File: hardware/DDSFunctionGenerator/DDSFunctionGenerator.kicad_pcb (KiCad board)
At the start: 2 copper layers, 100 x 100 mm, 83 parts, among them J1 Conn_Coaxial, Q1 Q_NPN_BEC, Q2 Q_NPN_BEC, Q3 Q_NPN_BEC, U1 TC1107-3.3VOA, U2 L7805, U3 L7805, U4 AD9832, U5 STM32F030K6Tx, Y1 Crystal

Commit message: draft of an amplifier
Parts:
- added C26: 100n, Capacitor_SMD:C_0805_2012Metric_Pad1.15x1.40mm_HandSolder, F.Cu at (95.0, 145.0)
- added C27: 100n, Capacitor_SMD:C_0805_2012Metric_Pad1.15x1.40mm_HandSolder, F.Cu at (97.6, 98.0)
- added C28: 100n, Capacitor_SMD:C_0805_2012Metric_Pad1.15x1.40mm_HandSolder, F.Cu at (92.9, 98.0)
- added C29: 100n, Capacitor_SMD:C_0805_2012Metric_Pad1.15x1.40mm_HandSolder, F.Cu at (92.9, 100.9)
- added C30: 100n, Capacitor_SMD:C_0805_2012Metric_Pad1.15x1.40mm_HandSolder, F.Cu at (92.9, 103.9)
- added C31: 100n, Capacitor_SMD:C_0805_2012Metric_Pad1.15x1.40mm_HandSolder, F.Cu at (102.4, 98.0)
- added C32: 100n, Capacitor_SMD:C_0805_2012Metric_Pad1.15x1.40mm_HandSolder, F.Cu at (100.0, 108.0)
- added C33: 100n, Capacitor_SMD:C_0805_2012Metric_Pad1.15x1.40mm_HandSolder, F.Cu at (107.3, 103.0)
- added C34: 100n, Capacitor_SMD:C_0805_2012Metric_Pad1.15x1.40mm_HandSolder, F.Cu at (104.8, 108.0)
- added C35: 100n, Capacitor_SMD:C_0805_2012Metric_Pad1.15x1.40mm_HandSolder, F.Cu at (109.5, 106.0)
- added C36: 100n, Capacitor_SMD:C_0805_2012Metric_Pad1.15x1.40mm_HandSolder, F.Cu at (109.5, 109.0)
- added D4: LED, LED_SMD:LED_0805_2012Metric, F.Cu at (99.6, 145.0)
- added J2: USB_B_Micro, Connector_USB:USB_Micro-B_Molex_47346-0001, F.Cu at (97.8, 139.1)
- added L9: 4u7, Inductor_SMD:L_1812_4532Metric_Pad1.30x3.40mm_HandSolder, F.Cu at (101.3, 104.0)
- added R31: 510R, Resistor_SMD:R_0805_2012Metric_Pad1.15x1.40mm_HandSolder, F.Cu at (105.2, 142.1)
- added SW1: Rotary_Encoder_Switch, Rotary_Encoder:RotaryEncoder_Alps_EC12E-Switch_Vertical_H20mm, F.Cu at (94.7, 121.2)
- added U6: FT200XD, Package_DFN_QFN:DFN-10-1EP_3x3mm_P0.5mm_EP1.55x2.48mm, F.Cu at (105.5, 138.2)
- added U7: AD8325, Package_SO:TSSOP-28_4.4x9.7mm_P0.65mm, F.Cu at (97.0, 90.0)

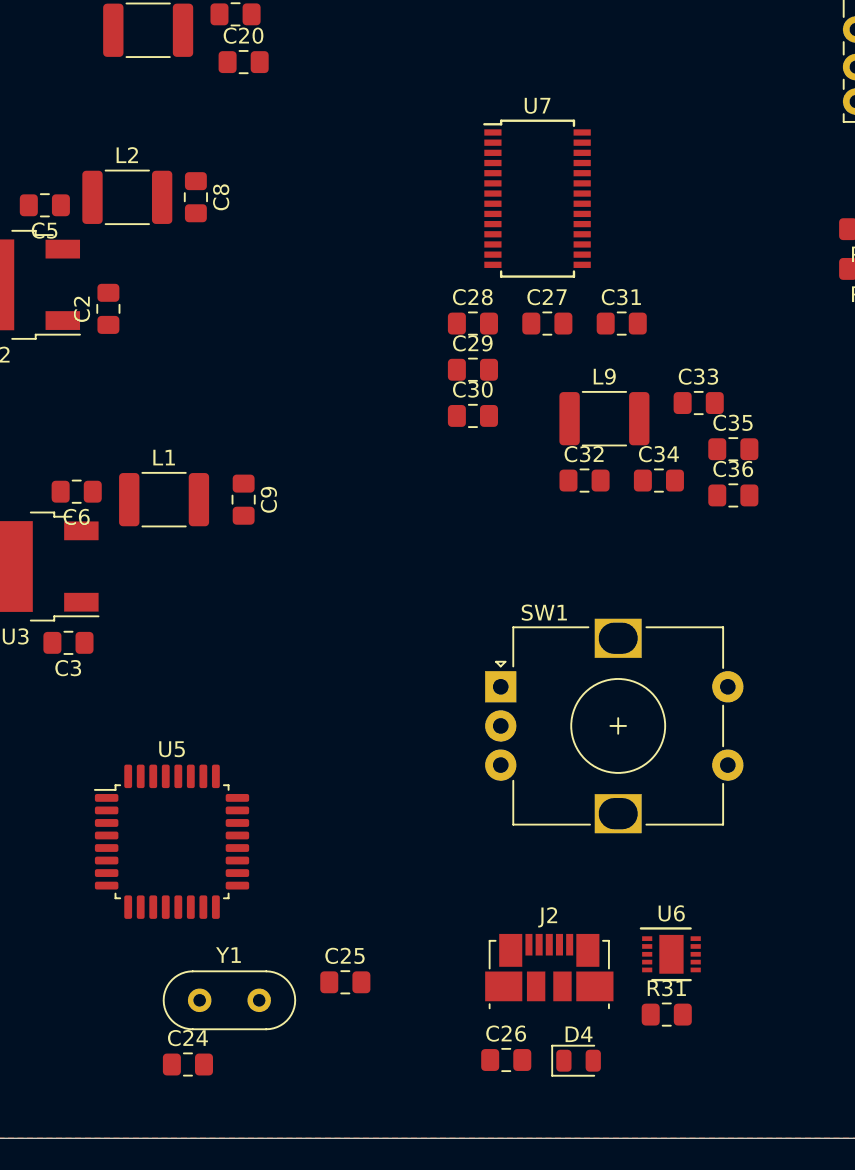
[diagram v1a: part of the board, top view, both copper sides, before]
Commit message: further refinement of amplifier
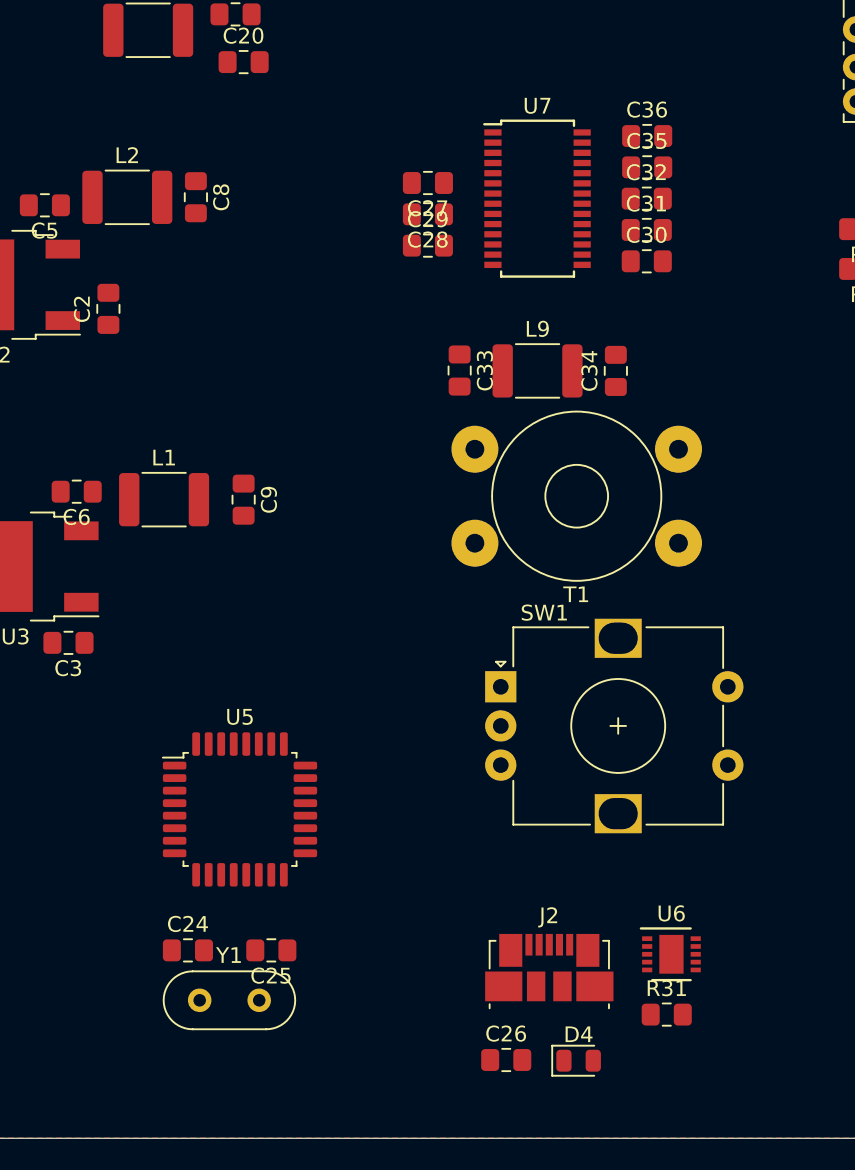
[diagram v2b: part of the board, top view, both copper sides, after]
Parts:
- added T1: Transformer_1P_1S, Transformer_THT:Transformer_Toroid_Horizontal_D10.5mm_Amidon-T37, F.Cu at (106.0, 106.0)
- C34: value 100n -> 10u/25V
- moved C36 23.6 mm to (104.0, 86.0)
- moved C35 18.8 mm to (104.0, 88.0)
- moved C32 18.4 mm to (104.0, 90.0)
- moved C33 15.4 mm to (92.0, 101.0), turned to 270 degrees
- moved C30 14.9 mm to (104.0, 94.0)
- moved C27 11.8 mm to (90.0, 89.0), turned to 180 degrees
- moved C29 8.43 mm to (90.0, 93.0)
- moved C28 7.54 mm to (90.0, 91.0), turned to 180 degrees
- moved C34 7.52 mm to (102.0, 101.0), turned to 90 degrees
- moved C24 7.29 mm to (74.7, 138.0)
- moved C31 6.19 mm to (104.0, 92.0)
- moved L9 5.25 mm to (97.0, 101.0)
- moved C25 5.15 mm to (80.0, 138.0), turned to 180 degrees
- moved U5 4.81 mm to (78.0, 129.0)
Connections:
- C30 pad 1: Net-(C30-Pad1) -> Net-(C27-Pad1)
- C31 pad 1: Net-(C30-Pad1) -> Net-(C27-Pad1)
- C32 pad 1: Net-(C30-Pad1) -> Net-(C27-Pad1)
- C35 pad 1: Net-(C30-Pad1) -> Net-(C27-Pad1)
- Rel1 pad 6: RF_DDS -> RF_FROM_AMPLIFIER
- U4 pad 8: (no net) -> SDATA
- U7 pad 14: (no net) -> Net-(T1-Pad2)
- U7 pad 15: (no net) -> Net-(T1-Pad1)
- U7 pad 19: Net-(C30-Pad1) -> Net-(C27-Pad1)
- U7 pad 2: (no net) -> SDATA
- U7 pad 20: Net-(C30-Pad1) -> Net-(C27-Pad1)
- U7 pad 23: Net-(C30-Pad1) -> Net-(C27-Pad1)
- U7 pad 24: (no net) -> GND
- U7 pad 26: (no net) -> RF_DDS
- U7 pad 27: Net-(C30-Pad1) -> Net-(C27-Pad1)
- U7 pad 4: (no net) -> GND
- U7 pad 8: (no net) -> GND

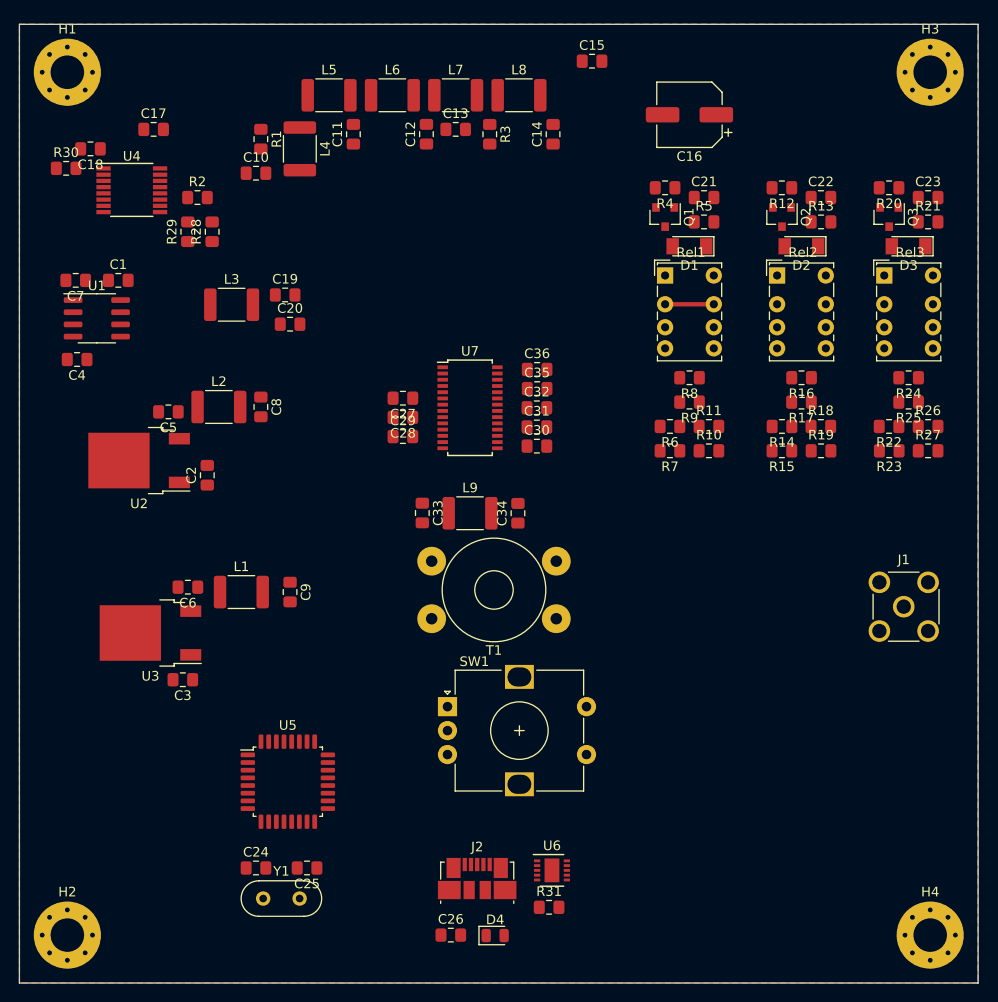
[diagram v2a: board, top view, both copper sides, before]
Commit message: modules placement improved
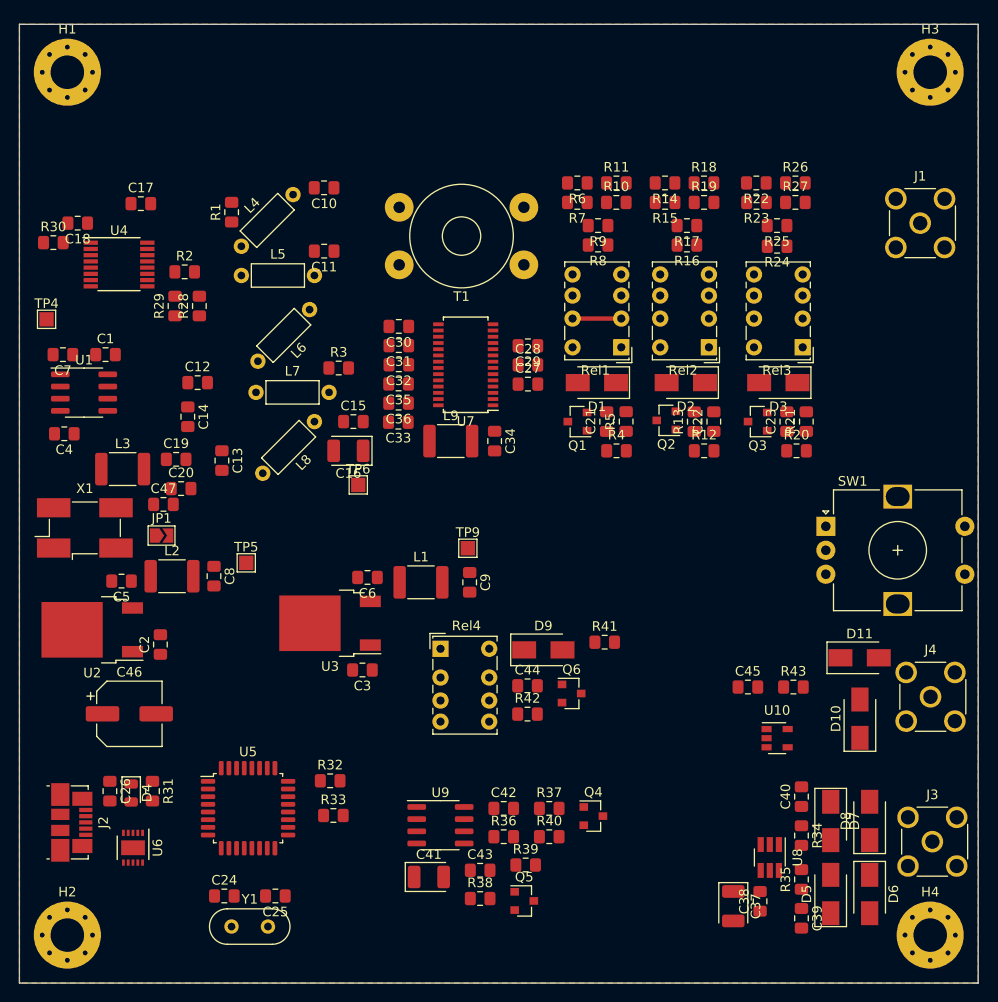
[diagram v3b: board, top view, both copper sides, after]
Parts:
- added C37: CP, Capacitor_Tantalum_SMD:CP_EIA-3528-21_Kemet-B, F.Cu at (124.5, 142.0)
- added C38: 100n, Capacitor_SMD:C_0805_2012Metric_Pad1.15x1.40mm_HandSolder, F.Cu at (127.3, 141.5)
- added C39: 100n, Capacitor_SMD:C_0805_2012Metric_Pad1.15x1.40mm_HandSolder, F.Cu at (131.6, 143.2)
- added C40: 100n, Capacitor_SMD:C_0805_2012Metric_Pad1.15x1.40mm_HandSolder, F.Cu at (131.6, 130.6)
- added C41: CP, Capacitor_Tantalum_SMD:CP_EIA-3528-21_Kemet-B, F.Cu at (92.7, 138.9)
- added C42: 100n, Capacitor_SMD:C_0805_2012Metric_Pad1.15x1.40mm_HandSolder, F.Cu at (100.5, 131.8)
- added C43: 100n, Capacitor_SMD:C_0805_2012Metric_Pad1.15x1.40mm_HandSolder, F.Cu at (98.1, 138.2)
- added C44: 1n, Capacitor_SMD:C_0805_2012Metric_Pad1.15x1.40mm_HandSolder, F.Cu at (103.0, 119.0)
- added C45: 100n, Capacitor_SMD:C_0805_2012Metric_Pad1.15x1.40mm_HandSolder, F.Cu at (126.0, 119.1)
- added C46: 22u/10V, Capacitor_SMD:CP_Elec_6.3x5.4, F.Cu at (61.5, 121.9)
- added C47: 15p, Capacitor_SMD:C_0805_2012Metric_Pad1.15x1.40mm_HandSolder, F.Cu at (65.0, 100.1)
- added D10: D_Schottky, Diode_SMD:D_SMA, F.Cu at (137.7, 122.4)
- added D11: D_Schottky, Diode_SMD:D_SMA, F.Cu at (137.6, 116.1)
- added D5: D_Schottky, Diode_SMD:D_SMA, F.Cu at (134.6, 140.7)
- added D6: D_Schottky, Diode_SMD:D_SMA, F.Cu at (138.7, 140.7)
- added D7: D_Schottky, Diode_SMD:D_SMA, F.Cu at (134.6, 133.1)
- added D8: D_Schottky, Diode_SMD:D_SMA, F.Cu at (138.7, 133.1)
- added D9: D, Diode_SMD:D_SMA, F.Cu at (104.6, 115.2)
- added J3: Conn_Coaxial, Connector_Coaxial:SMA_Molex_73251-2200_Horizontal, F.Cu at (145.2, 135.3)
- added J4: Conn_Coaxial, Connector_Coaxial:SMA_Molex_73251-2200_Horizontal, F.Cu at (145.0, 120.1)
- added JP1: SolderJumper_2_Open, Jumper:SolderJumper-2_P1.3mm_Open_TrianglePad1.0x1.5mm, F.Cu at (64.8, 103.3)
- added Q4: BC859, Package_TO_SOT_SMD:SOT-23, F.Cu at (109.9, 132.6)
- added Q5: BC848, Package_TO_SOT_SMD:SOT-23, F.Cu at (102.7, 141.4)
- added Q6: Q_NPN_BEC, Package_TO_SOT_SMD:SOT-23, F.Cu at (107.6, 119.8)
- added R32: 49R9, Resistor_SMD:R_0805_2012Metric_Pad1.15x1.40mm_HandSolder, F.Cu at (82.4, 128.9)
- added R33: 49R9, Resistor_SMD:R_0805_2012Metric_Pad1.15x1.40mm_HandSolder, F.Cu at (82.7, 132.5)
- added R34: 49R9, Resistor_SMD:R_0805_2012Metric_Pad1.15x1.40mm_HandSolder, F.Cu at (131.6, 134.6)
- added R35: 49R9, Resistor_SMD:R_0805_2012Metric_Pad1.15x1.40mm_HandSolder, F.Cu at (131.6, 139.2)
- added R36: 49R9, Resistor_SMD:R_0805_2012Metric_Pad1.15x1.40mm_HandSolder, F.Cu at (100.5, 134.7)
- added R37: 49R9, Resistor_SMD:R_0805_2012Metric_Pad1.15x1.40mm_HandSolder, F.Cu at (105.3, 131.8)
- added R38: 49R9, Resistor_SMD:R_0805_2012Metric_Pad1.15x1.40mm_HandSolder, F.Cu at (98.1, 141.2)
- added R39: 49R9, Resistor_SMD:R_0805_2012Metric_Pad1.15x1.40mm_HandSolder, F.Cu at (102.8, 137.7)
- added R40: 49R9, Resistor_SMD:R_0805_2012Metric_Pad1.15x1.40mm_HandSolder, F.Cu at (105.3, 134.7)
- added R41: 2k2, Resistor_SMD:R_0805_2012Metric_Pad1.15x1.40mm_HandSolder, F.Cu at (111.0, 114.4)
- added R42: 10k, Resistor_SMD:R_0805_2012Metric_Pad1.15x1.40mm_HandSolder, F.Cu at (103.0, 121.9)
- added R43: 10R, Resistor_SMD:R_0805_2012Metric_Pad1.15x1.40mm_HandSolder, F.Cu at (130.7, 119.1)
- added Rel4: RSM850B-6112-85-1005, Relay_THT:Relay_DPDT_Omron_G6K-2P-Y, F.Cu at (93.9, 115.1)
- added TP4: TestPoint, TestPoint:TestPoint_Pad_1.5x1.5mm, F.Cu at (52.8, 80.8)
- added TP5: TestPoint, TestPoint:TestPoint_Pad_1.5x1.5mm, F.Cu at (73.7, 106.2)
- added TP6: TestPoint, TestPoint:TestPoint_Pad_1.5x1.5mm, F.Cu at (85.3, 98.0)
- added TP9: TestPoint, TestPoint:TestPoint_Pad_1.5x1.5mm, F.Cu at (96.8, 104.6)
- added U10: 74HCT1G86, Package_TO_SOT_SMD:SOT-23-5, F.Cu at (129.0, 124.5)
- added U8: MCP3425A0T-ECH, Package_TO_SOT_SMD:SOT-23-6_Handsoldering, F.Cu at (128.3, 136.9)
- added U9: LM358, Package_SO:SOIC-8_3.9x4.9mm_P1.27mm, F.Cu at (93.9, 133.5)
- added X1: XO91, Oscillator:Oscillator_SMD_EuroQuartz_XO91-4Pin_7.0x5.0mm_HandSoldering, F.Cu at (56.8, 102.5)
- C16: footprint Capacitor_SMD:CP_Elec_6.3x5.4 -> Capacitor_Tantalum_SMD:CP_EIA-3528-21_Kemet-B
- D1, D2, D3: footprint Diode_SMD:D_MiniMELF -> Diode_SMD:D_SMA
- L4, L5, L6, L7, L8: footprint Inductor_SMD:L_1812_4532Metric_Pad1.30x3.40mm_HandSolder -> Inductor_THT:L_Axial_L5.3mm_D2.2mm_P7.62mm_Horizontal_Vishay_IM-1
- moved C16 49.9 mm to (84.3, 94.5)
- moved C14 48.2 mm to (67.6, 90.9), turned to 270 degrees
- moved C15 45.1 mm to (84.8, 91.4)
- moved U6 43.8 mm to (61.8, 135.9), turned to 270 degrees
- moved SW1 43.7 mm to (134.1, 102.4)
- moved R31 43.1 mm to (63.9, 130.0), turned to 270 degrees
- moved J2 42.7 mm to (55.5, 133.2), turned to 270 degrees
- moved C13 42.3 mm to (71.1, 95.5), turned to 270 degrees
- moved D4 40.8 mm to (61.7, 130.2), turned to 270 degrees
- moved L8 40.2 mm to (80.8, 91.4), turned to 225 degrees
- moved J1 40.0 mm to (144.0, 70.7)
- moved C26 38.6 mm to (59.4, 130.0), turned to 270 degrees
- moved L7 37.3 mm to (74.7, 88.4)
- moved T1 37.1 mm to (102.6, 69.1)
- moved C12 35.2 mm to (68.6, 87.4), turned to 0 degrees
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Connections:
- C17 pad 1: Net-(C17-Pad1) -> 5V_ANALOG
- C33 pad 1: Net-(C33-Pad1) -> 5V_ANALOG
- C34 pad 1: Net-(C34-Pad1) -> Net-(C27-Pad1)
- C8 pad 1: Net-(C17-Pad1) -> 5V_ANALOG
- L2 pad 2: Net-(C17-Pad1) -> 5V_ANALOG
- L9 pad 1: Net-(C33-Pad1) -> 5V_ANALOG
- L9 pad 2: Net-(C34-Pad1) -> Net-(C27-Pad1)
- R4 pad 2: (no net) -> REL_1
- Rel1 pad 1: Net-(D1-Pad2) -> +9V
- Rel1 pad 3: Net-(Rel1-Pad3) -> RF_FROM_AMPLIFIER
- Rel1 pad 4: Net-(R6-Pad1) -> Net-(R10-Pad1)
- Rel1 pad 5: Net-(R10-Pad1) -> Net-(R6-Pad1)
- Rel1 pad 6: RF_FROM_AMPLIFIER -> Net-(Rel1-Pad6)
- Rel1 pad 8: +9V -> Net-(D1-Pad2)
- Rel2 pad 1: Net-(D2-Pad2) -> +9V
- Rel2 pad 3: Net-(Rel2-Pad3) -> Net-(Rel1-Pad6)
- Rel2 pad 4: Net-(R14-Pad1) -> Net-(R16-Pad1)
- Rel2 pad 5: Net-(R16-Pad1) -> Net-(R14-Pad1)
- Rel2 pad 6: Net-(Rel1-Pad3) -> Net-(Rel2-Pad6)
- Rel2 pad 8: +9V -> Net-(D2-Pad2)
- Rel3 pad 1: Net-(D3-Pad2) -> +9V
- Rel3 pad 3: Net-(J1-Pad1) -> Net-(Rel2-Pad6)
- Rel3 pad 4: Net-(R22-Pad1) -> Net-(R24-Pad1)
- Rel3 pad 5: Net-(R24-Pad1) -> Net-(R22-Pad1)
- Rel3 pad 6: Net-(Rel2-Pad3) -> Net-(J1-Pad1)
- Rel3 pad 8: +9V -> Net-(D3-Pad2)
- T1 pad 3: GND -> RF_FROM_AMPLIFIER
- T1 pad 4: RF_FROM_AMPLIFIER -> GND
- U4 pad 15: Net-(C17-Pad1) -> 5V_ANALOG
- U4 pad 6: Net-(C7-Pad2) -> Net-(C47-Pad2)
- U7 pad 14: Net-(T1-Pad2) -> Net-(T1-Pad1)
- U7 pad 15: Net-(T1-Pad1) -> Net-(T1-Pad2)

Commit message: 3d models added
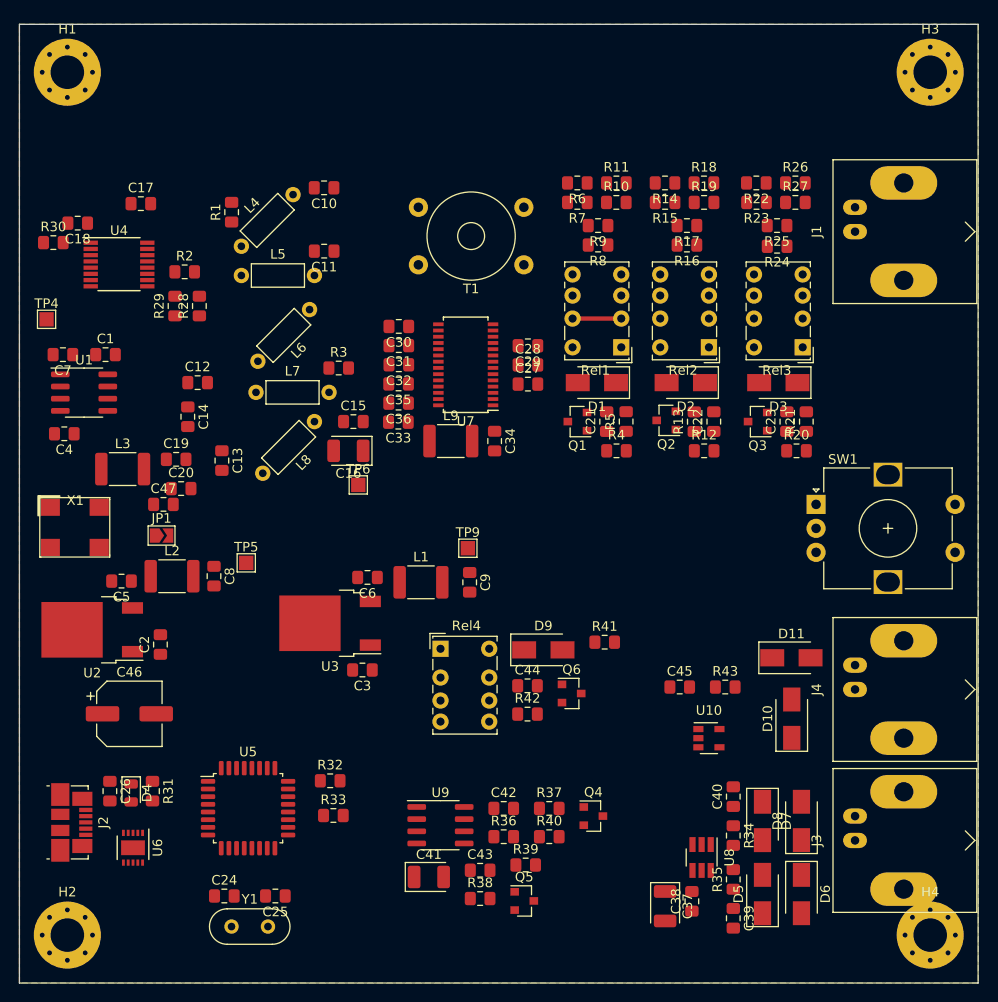
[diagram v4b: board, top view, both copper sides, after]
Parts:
- J1, J3, J4: footprint Connector_Coaxial:SMA_Molex_73251-2200_Horizontal -> Connector_Coaxial:BNC_Amphenol_B6252HB-NPP3G-50_Horizontal
- T1: footprint Transformer_THT:Transformer_Toroid_Horizontal_D10.5mm_Amidon-T37 -> Transformer_THT:Transformer_Toroid_Horizontal_D9.0mm_Amidon-T30
- X1: footprint Oscillator:Oscillator_SMD_EuroQuartz_XO91-4Pin_7.0x5.0mm_HandSoldering -> DDSFunctionGenerator:LF SPXO018035
- moved J3 8.07 mm to (137.2, 135.1)
- moved J4 7.91 mm to (137.2, 119.4)
- moved C38 7.11 mm to (120.1, 141.5)
- moved C39 7.11 mm to (124.5, 143.2)
- moved C40 7.11 mm to (124.5, 130.6)
- moved D5 7.11 mm to (127.5, 140.7)
- moved D7 7.11 mm to (127.5, 133.1)
- moved R34 7.11 mm to (124.5, 134.6)
- moved R35 7.11 mm to (124.5, 139.2)
- moved R43 7.11 mm to (123.6, 119.1)
- moved U10 7.11 mm to (121.9, 124.5)
- moved U8 7.11 mm to (121.2, 136.9)
- moved C37 7.11 mm to (117.3, 142.0)
- moved C45 7.11 mm to (118.9, 119.1)
- moved D10 7.11 mm to (130.6, 122.4)
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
